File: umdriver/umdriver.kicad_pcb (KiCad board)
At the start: 2 copper layers, 100 x 90 mm, 79 parts, among them J1 SWD, J3 Isolated rs485, K1 FINDER-32.21-x000, Q1 Q_NMOS_GDS, SW1 SW_Reset, SW2 SW_Test, U1 STGIPQ8C60T, U2 NCP718, U3 ATSAMD21G18A-AUT, U4 ISO3088DW, Y1 32.768

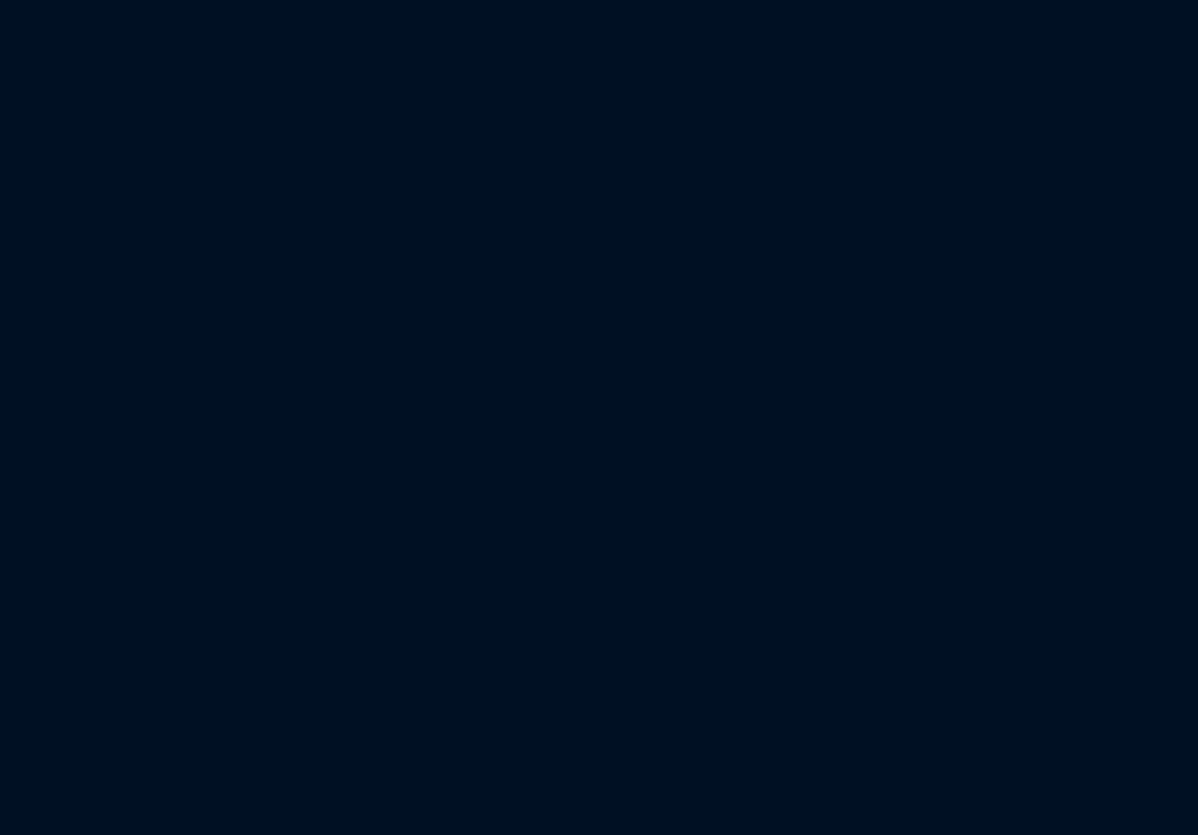
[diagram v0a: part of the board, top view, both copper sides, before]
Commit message: Add a power supply. Not clear yet if it is sufficient current-vise
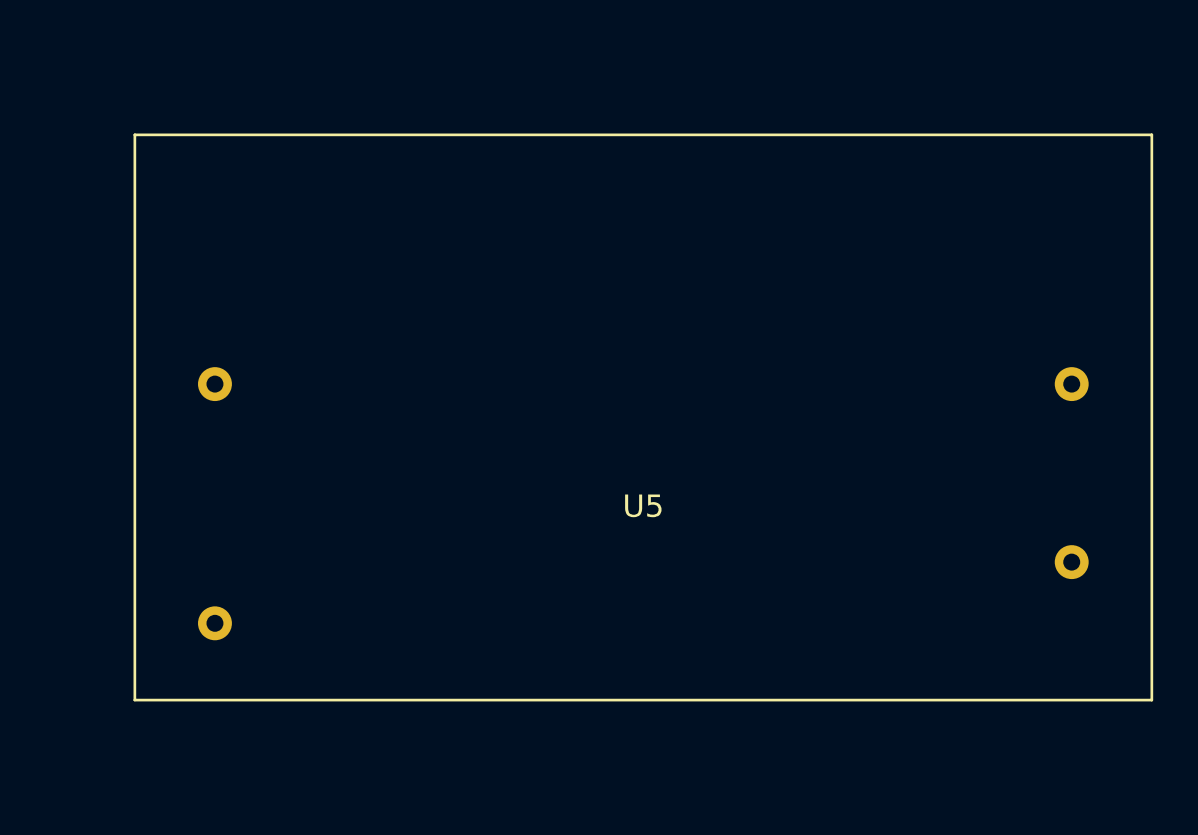
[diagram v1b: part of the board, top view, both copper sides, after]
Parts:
- added U5: PSU, umdriver:IRM-10-15, F.Cu at (168.9, 99.0)
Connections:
- net /Microcontroller/D+ renamed Net-(U3-Pad34)
- net /Microcontroller/D- renamed Net-(U3-Pad33)
- net /Power Input/LINE_L renamed /LINE_L
- net /Power Input/LINE_N renamed /LINE_N
- R15 pad 2: /Power Input/INRUSH_BYPASS -> /INRUSH_BYPASS
- R16 pad 1: /Power Input/INRUSH_BYPASS -> /INRUSH_BYPASS
- R24 pad 2: /Power Input/DC_BUS_MON -> /DC_BUS_MON
- R25 pad 1: /Power Input/DC_BUS_MON -> /DC_BUS_MON
- U3 pad 11: Net-(U3-Pad11) -> /ISENSE
- U3 pad 12: Net-(U3-Pad12) -> /NTC
- U3 pad 16: Net-(U3-Pad16) -> /HINW
- U3 pad 21: Net-(U3-Pad21) -> /LINW
- U3 pad 22: Net-(U3-Pad22) -> /HINV
- U3 pad 23: Net-(U3-Pad23) -> /LINV
- U3 pad 24: Net-(U3-Pad24) -> /LINU
- U3 pad 25: Net-(U3-Pad25) -> /HINU
- U3 pad 27: Net-(U3-Pad27) -> /INRUSH_BYPASS
- U3 pad 3: /Microcontroller/BATT_MON -> /DC_BUS_MON

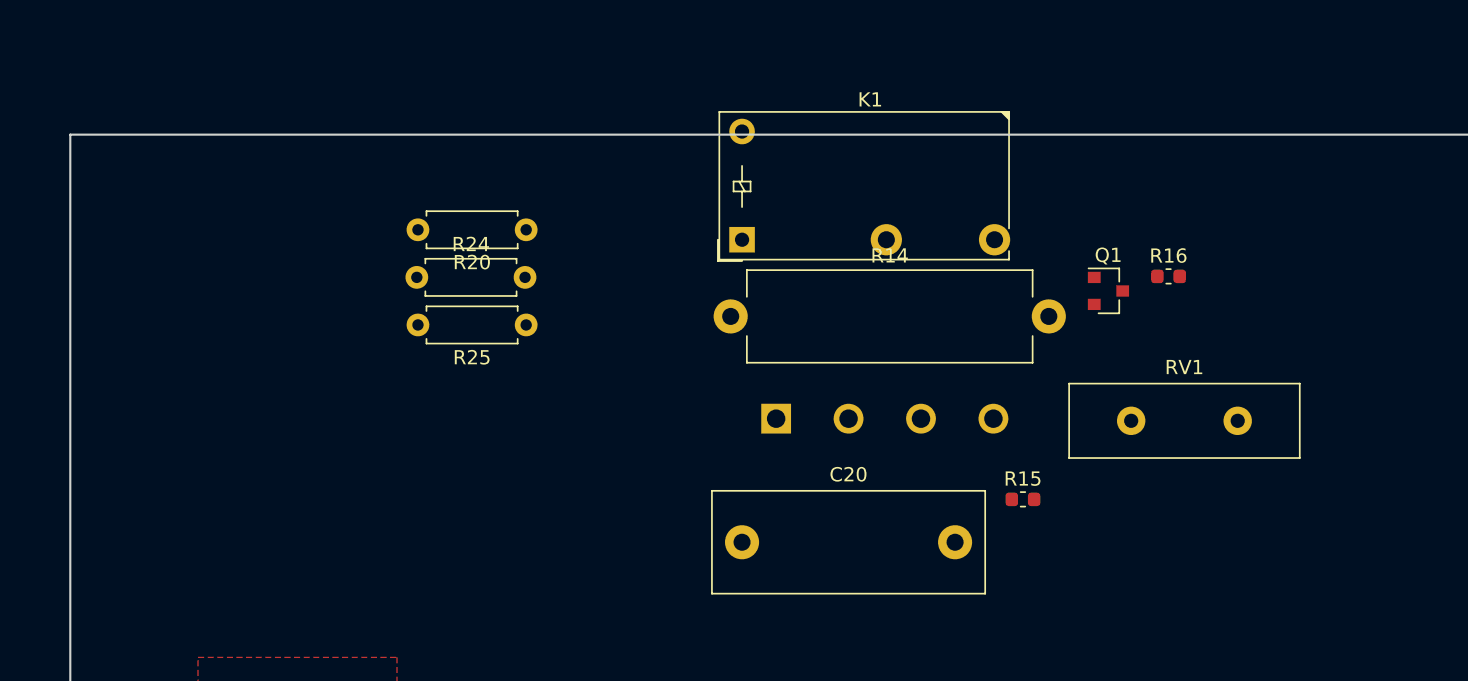
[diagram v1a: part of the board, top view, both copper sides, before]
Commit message: Source the most of the components, update footprints
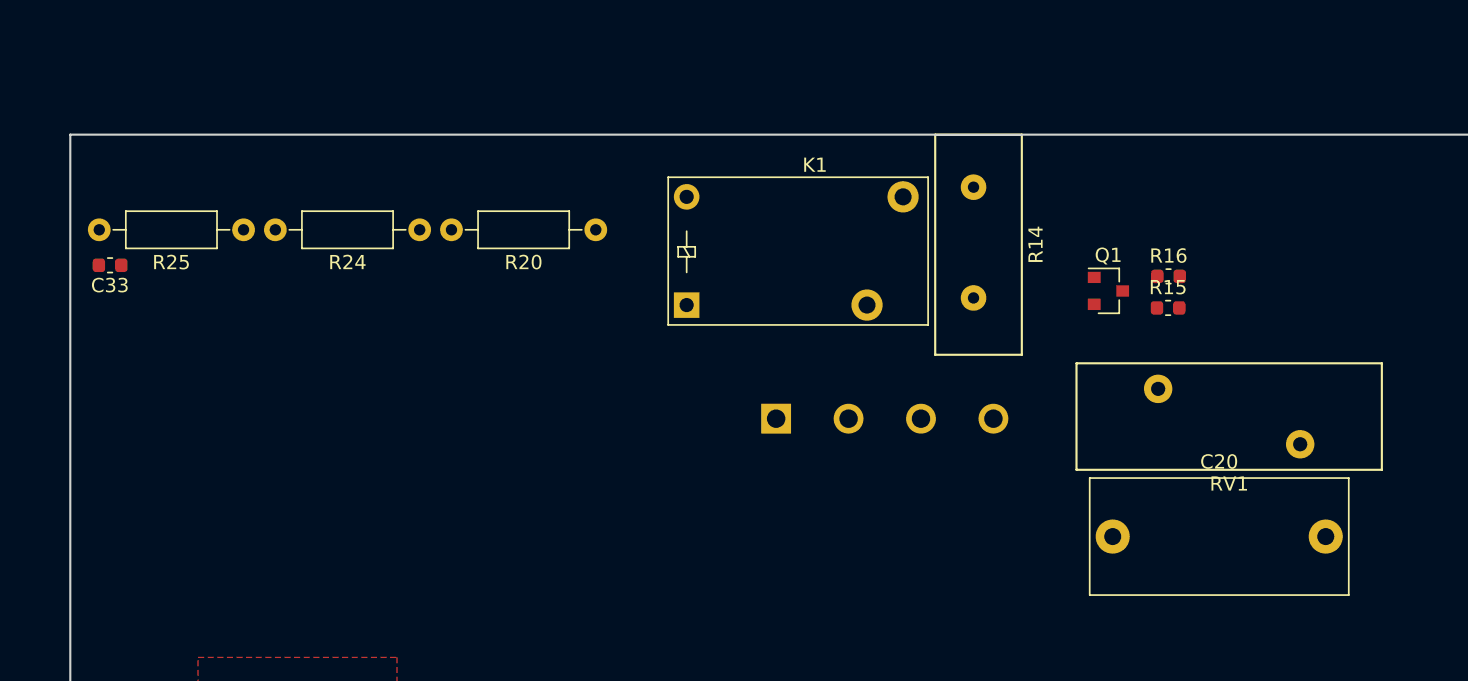
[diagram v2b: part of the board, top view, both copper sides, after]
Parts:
- added C33: 1u, Capacitor_SMD:C_0603_1608Metric, F.Cu at (52.8, 49.2)
- C20: footprint Capacitor_THT:C_Rect_L19.0mm_W7.0mm_P15.00mm_MKS4 -> Capacitor_THT:C_Rect_L18.0mm_W8.0mm_P15.00mm_FKS3_FKP3
- K1: value FINDER-32.21-x000 -> SPST; footprint Relay_THT:Relay_SPST_Finder_32.21-x300 -> umdriver:Relay_SPST
- R14: value R -> 1k; footprint Resistors_THT:R_Axial_Power_L20.0mm_W6.4mm_P22.40mm -> Varistors:RV_Disc_D15.5_W6.1_P7.5
- R20, R24: value R -> 100k; footprint Resistors_THT:R_Axial_DIN0207_L6.3mm_D2.5mm_P7.62mm_Horizontal -> Resistors_THT:R_Axial_DIN0207_L6.3mm_D2.5mm_P10.16mm_Horizontal
- R25: value R -> 1.8k; footprint Resistors_THT:R_Axial_DIN0207_L6.3mm_D2.5mm_P7.62mm_Horizontal -> Resistors_THT:R_Axial_DIN0207_L6.3mm_D2.5mm_P10.16mm_Horizontal
- RV1: footprint Capacitor_THT:C_Disc_D16.0mm_W5.0mm_P7.50mm -> Varistors:RV_Disc_D21.5_W7.5_P10
- moved C20 26.1 mm to (123.4, 68.3)
- moved R25 21.0 mm to (62.2, 46.7)
- moved R14 17.1 mm to (113.6, 51.5), turned to 90 degrees
- moved R15 16.9 mm to (127.3, 52.2)
- moved K1 6.03 mm to (93.4, 52.0)
- moved R20 4.90 mm to (87.0, 46.7)
- moved R24 3.36 mm to (74.6, 46.7), turned to 180 degrees
- moved RV1 2.94 mm to (126.6, 57.9)

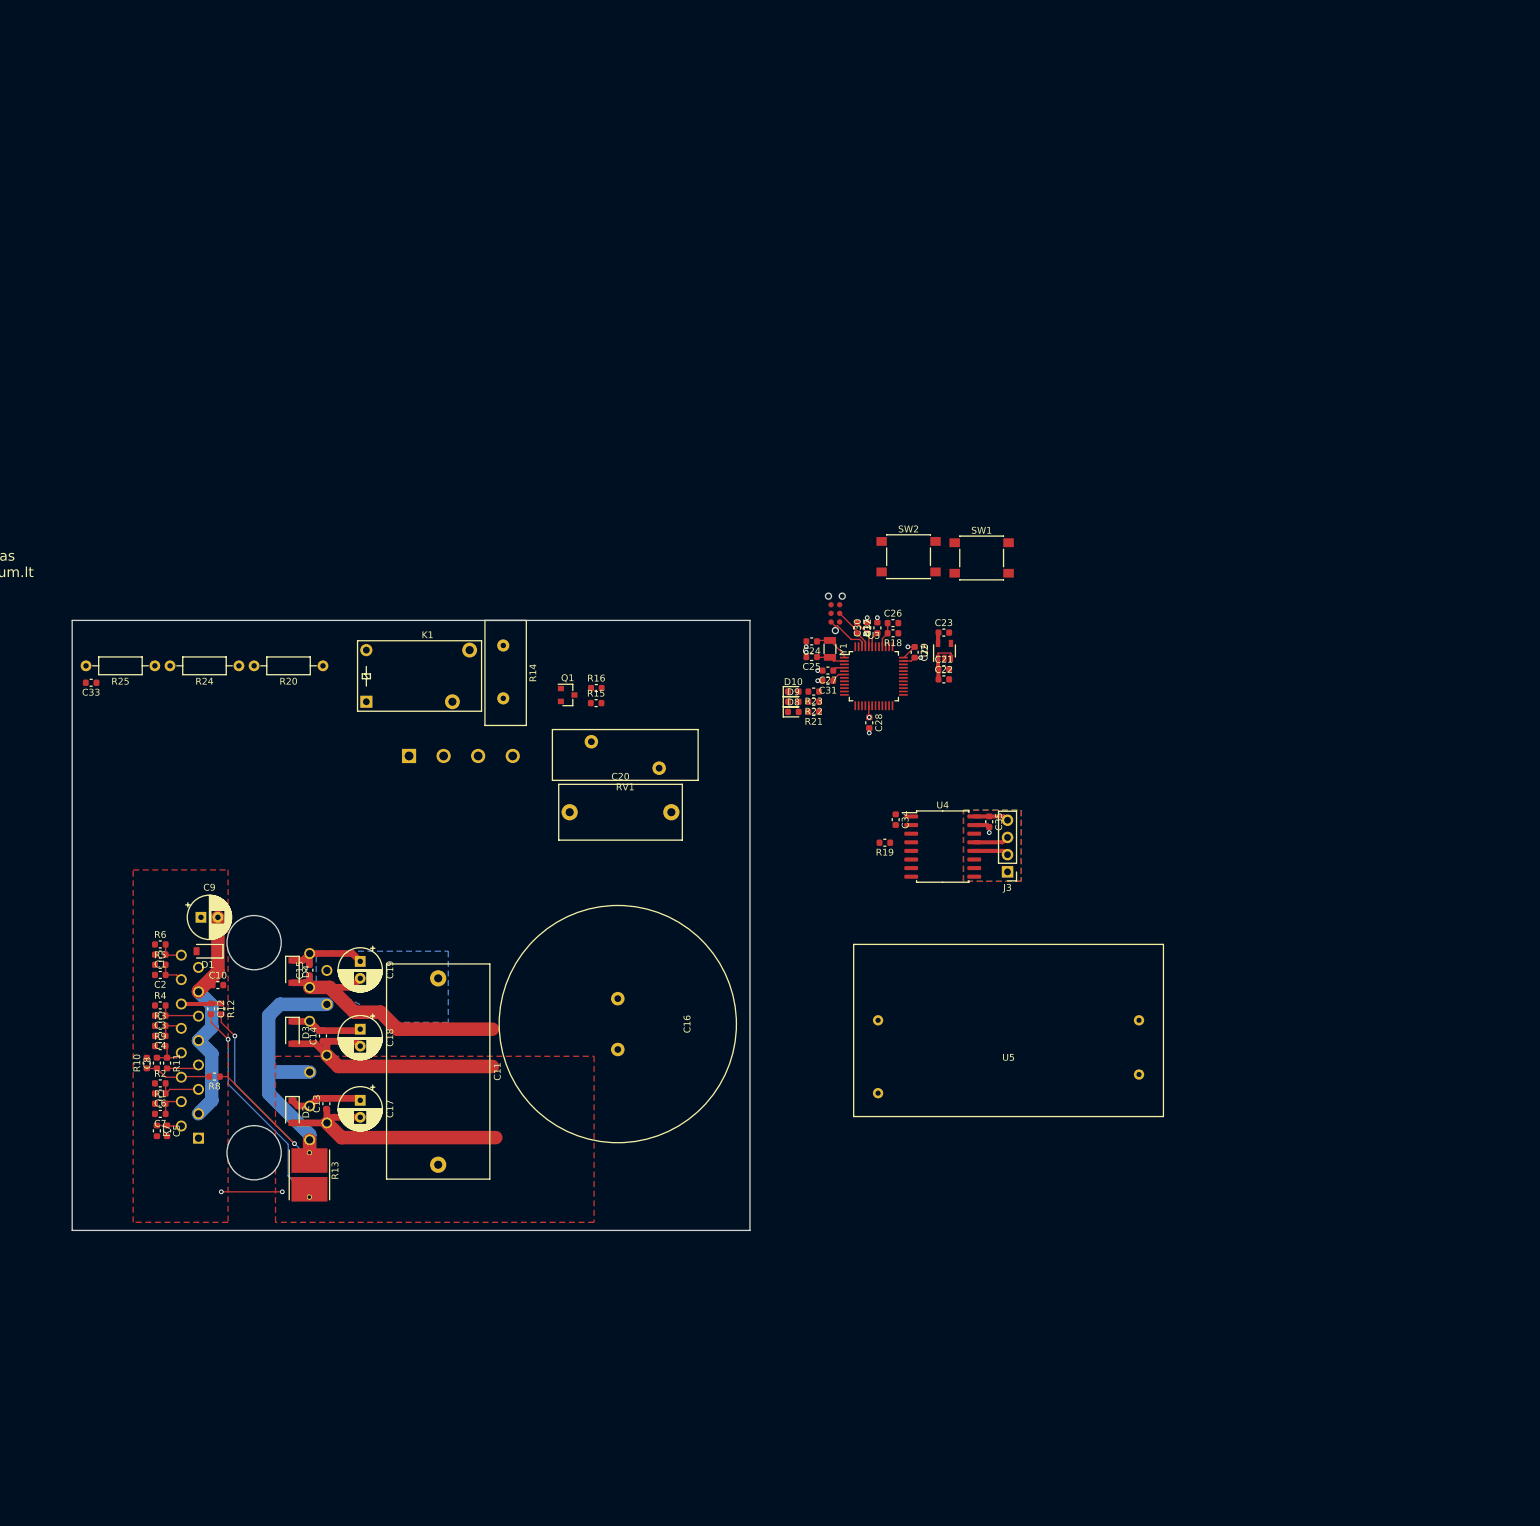
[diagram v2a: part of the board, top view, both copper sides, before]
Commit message: Source bridge rectifier, import board shape, start placing and routing on the real shape
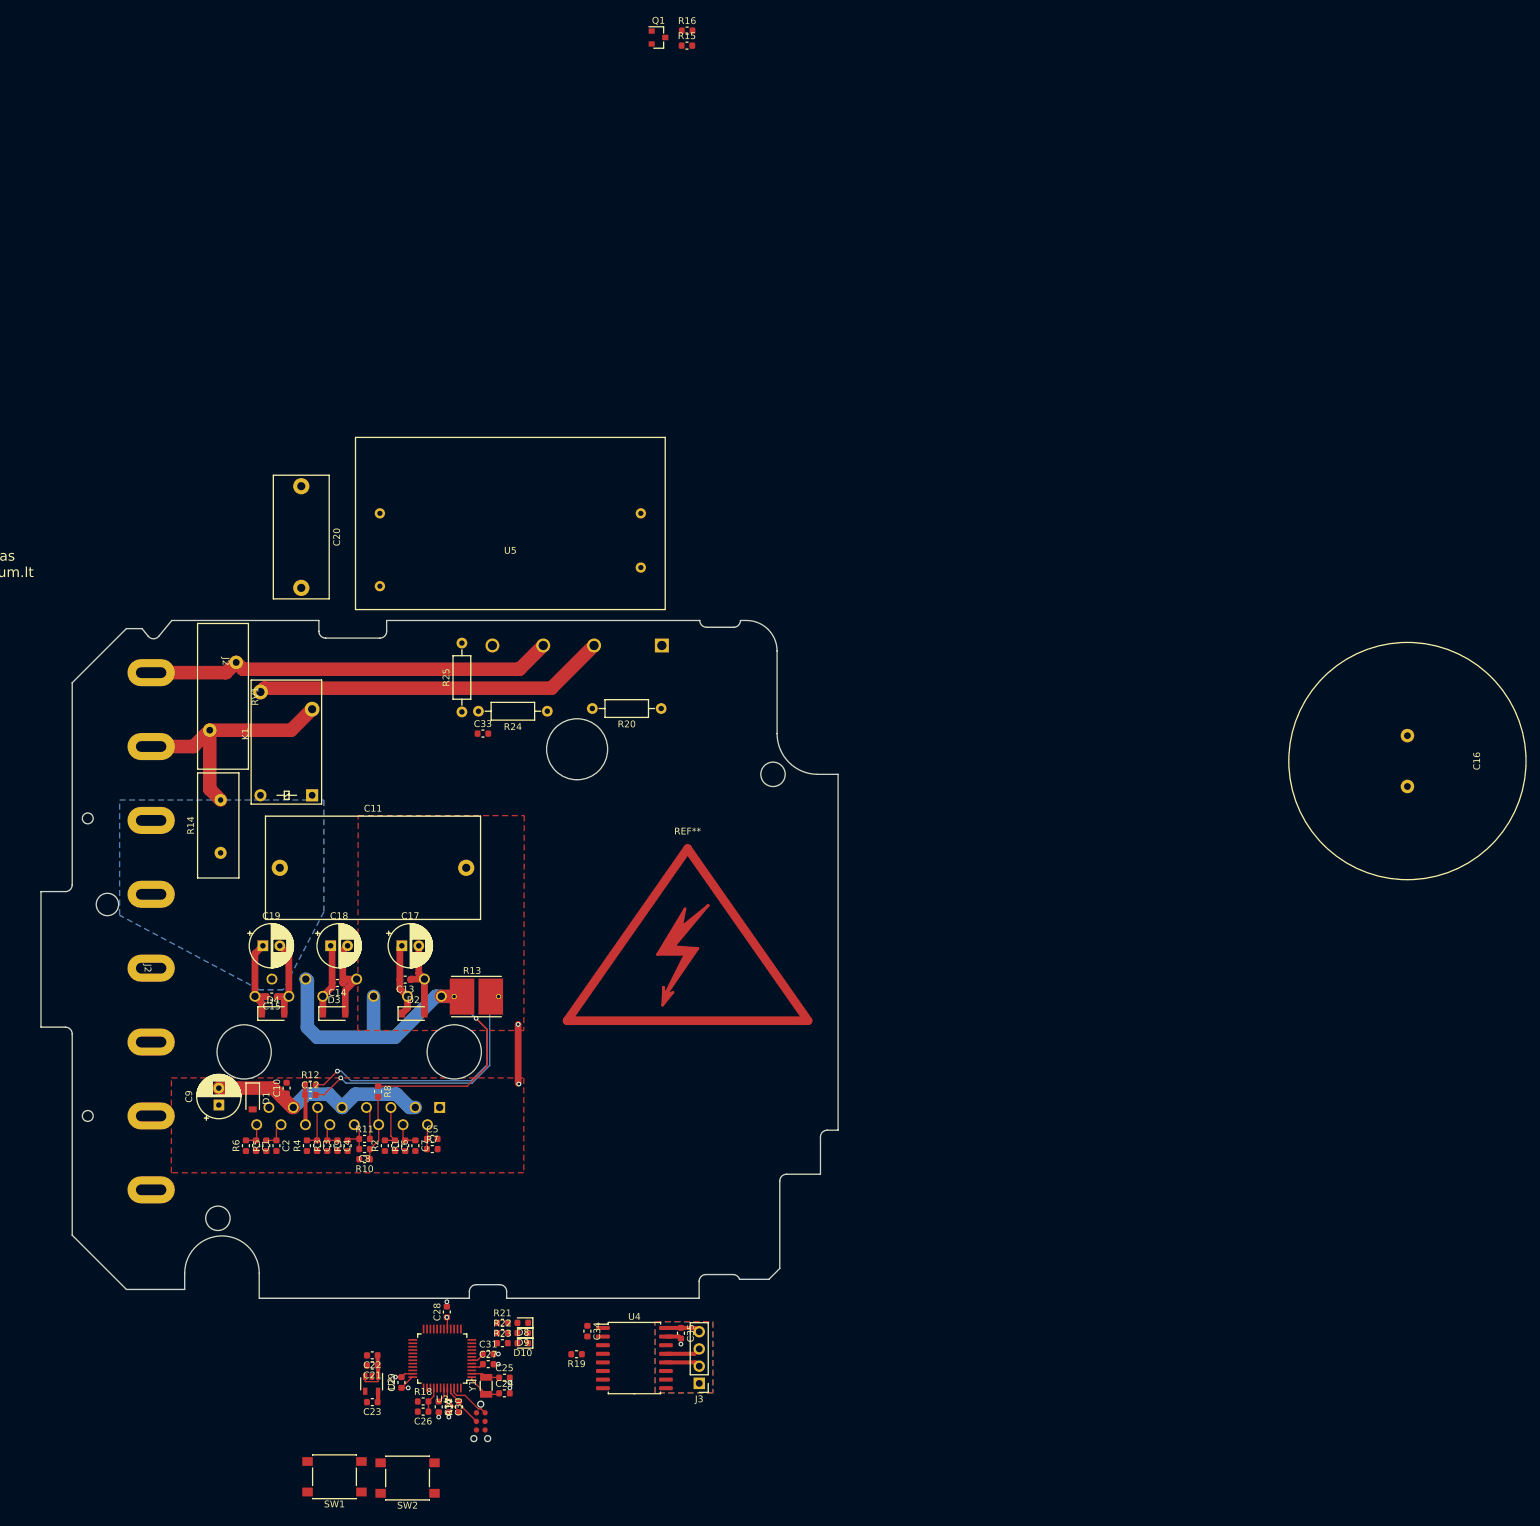
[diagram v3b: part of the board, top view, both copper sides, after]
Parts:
- added J2: Conn_01x08, umdriver:TB-YAG-8P, F.Cu at (61.6, 47.7)
- added REF**: Symbol_HighVoltage_Type2_CopperTop_Big, Symbols:Symbol_HighVoltage_Type2_CopperTop_Big, F.Cu at (140.8, 88.9)
- D5: footprint Diodes_THT:Diode_Bridge_18.5x5.5 -> umdriver:DIOB_GSIB2560-E3-45
- moved SW1 165.8 mm to (88.7, 166.3), turned to 180 degrees
- moved SW2 154.7 mm to (99.5, 166.5), turned to 180 degrees
- moved C23 141.4 mm to (94.3, 155.3), turned to 180 degrees
- moved U2 137.2 mm to (94.2, 152.6), turned to -90 degrees
- moved C26 135.4 mm to (101.8, 156.7), turned to 180 degrees
- moved C21 132.9 mm to (94.3, 149.9), turned to 180 degrees
- moved R18 132.9 mm to (101.8, 155.2), turned to 0 degrees
- moved C32 131.9 mm to (104.1, 156.0), turned to -90 degrees
- moved C29 131.7 mm to (98.6, 152.4), turned to 90 degrees
- moved C22 130.6 mm to (94.3, 148.4), turned to 180 degrees
- moved C30 130.5 mm to (105.6, 156.0), turned to -90 degrees
- moved R17 129.1 mm to (107.1, 156.0), turned to 90 degrees
- moved J1 125.6 mm to (110.3, 155.6), turned to -90 degrees
- moved C16 122.8 mm to (247.0, 57.0)
- moved Y1 120.0 mm to (111.1, 152.9), turned to 90 degrees
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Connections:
- K1 pad 14: Net-(D5-Pad2) -> Net-(D5-PadAC1)
- R14 pad 2: Net-(D5-Pad2) -> Net-(D5-PadAC1)
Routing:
- net /LINE_N: track 0.00 -> 60.3 mm
- net Net-(D5-PadAC1): track 0.00 -> 52.1 mm
- net /LINE_L: track 0.00 -> 37.0 mm
- net /UOUT: track 42.1 -> 12.6 mm
- net /VSHUNT: track 80.7 -> 108.6 mm
- net /WOUT: track 38.2 -> 12.4 mm
- net /VOUT: track 39.0 -> 13.9 mm
- net GND: track 44.8 -> 50.4 mm
- added copper zone on In2.Cu, net /UOUT
- added copper zone on In1.Cu, net /VOUT
- added copper zone on In2.Cu, net /WOUT
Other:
- board size 100 x 90 mm -> 117.6 x 100 mm
- copper layers 2 -> 4
- net class Hi Voltage added: clearance 0.8, trace_width 2, via_dia 2, via_drill 0.8
